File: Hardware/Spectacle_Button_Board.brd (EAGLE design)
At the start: 44.5 x 73.7 mm, 45 parts, among them J17 AUDIO-JACK3, J19 FTDI_DEVICE, U1 CY8C4146LQI-S422, U2 3.3V/150mA

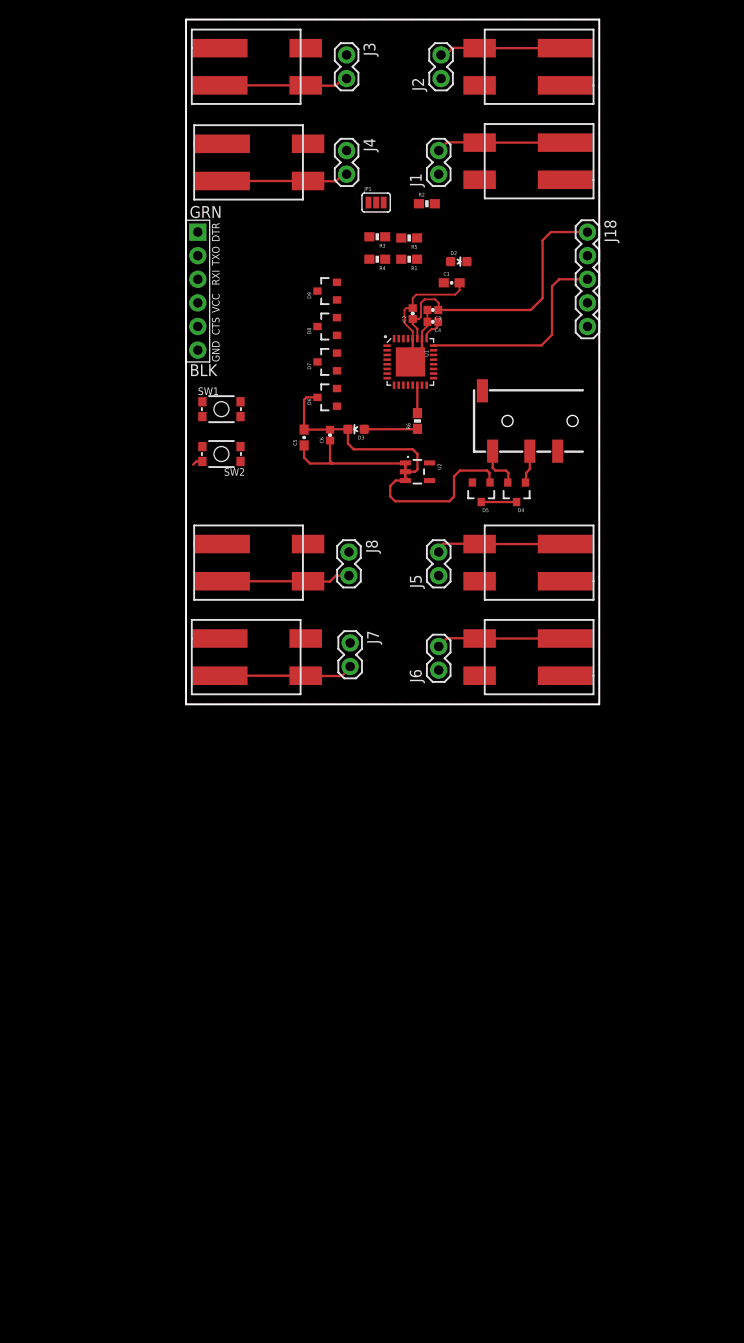
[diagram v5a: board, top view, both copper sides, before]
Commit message: Added second trrs connector
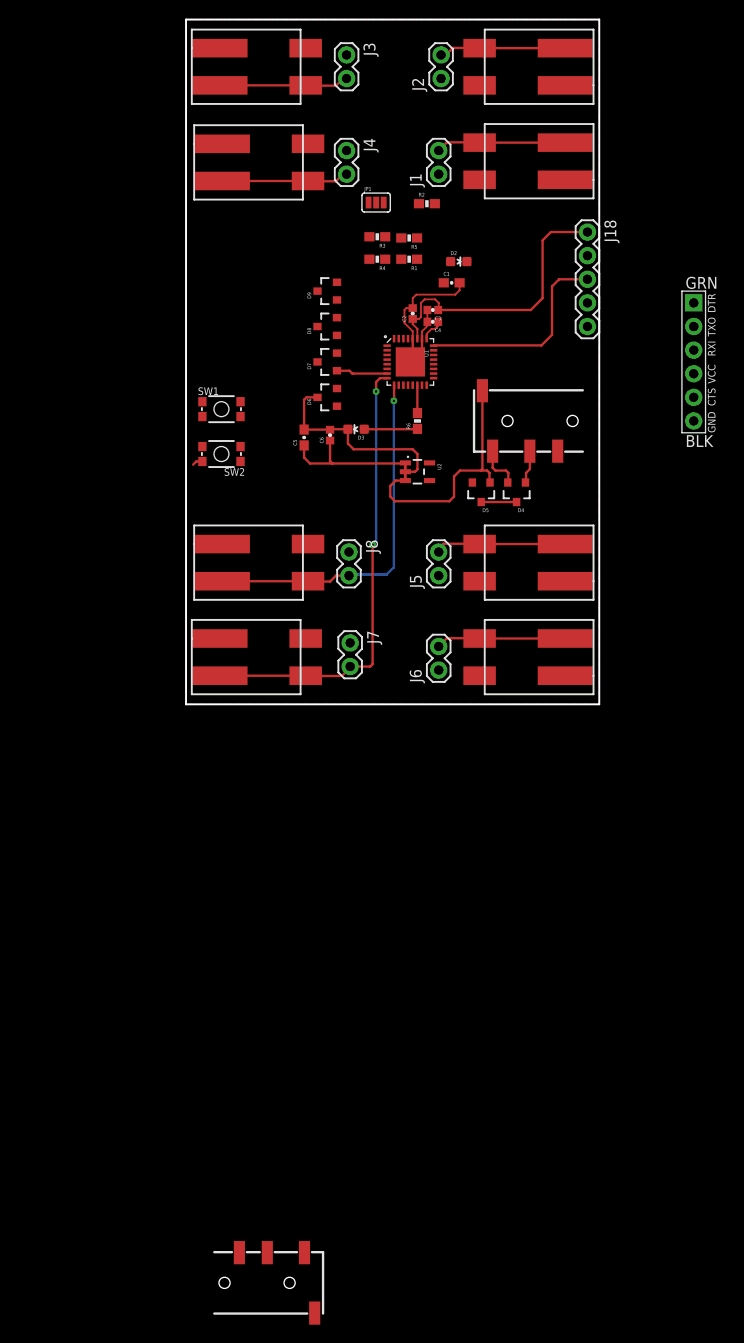
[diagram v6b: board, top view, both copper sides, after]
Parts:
- added J20: AUDIO-JACK3, SparkFun-Connectors:AUDIO-JACK-TRRS-SMD
- moved J19 53.9 mm to (22.9, 27.9)
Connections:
- net GND: now also J20.RING2
- net VIN: now also J20.EARTH
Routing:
- net IN_6: track 14.5 -> 48.9 mm, vias 0 -> 2
- net IN_7: track 13.9 -> 38.7 mm, vias 0 -> 1
- net VIN: track 34.6 -> 43.3 mm
- net IN_5: track 14.0 -> 19.6 mm
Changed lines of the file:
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@@
 <element name="JP1" library="SparkFun-Passives" package="PAD-JUMPER-3-NC_BY_PASTE_YES_SILK_FULL_BOX" value="JUMPER-PAD-3-NC_BY_PASTE" x="-11.303" y="45.085"/>
 <element name="J18" library="SparkFun-Connectors" package="1X05" value="" x="11.43" y="41.91" rot="R270"/>
-<element name="J19" library="SparkFun-Connectors" package="FTDI_DEVICE_SIDE" value="FTDI_DEVICE" x="-30.48" y="35.56" rot="R270"/>
+<element name="J19" library="SparkFun-Connectors" package="FTDI_DEVICE_SIDE" value="FTDI_DEVICE" x="22.86" y="27.94" rot="R270"/>
 <element name="D2" library="SparkFun-LED" package="LED-0603" value="RED" x="-2.413" y="38.735" rot="R270">
 <attribute name="PROD_ID" value="DIO-00819" x="-2.413" y="38.735" size="1.778" layer="27" font="vector" ratio="15" rot="R270" display="off"/>
@@
 <attribute name="PROD_ID" value="DIO-12501" x="-16.51" y="35.56" size="1.778" layer="27" font="vector" ratio="15" rot="R90" display="off"/>
 </element>
+<element name="J20" library="SparkFun-Connectors" package="AUDIO-JACK-TRRS-SMD" value="AUDIO-JACK3" x="-29.21" y="-71.12"/>
 </elements>
 <signals>
@@
 <vertex x="12.7" y="64.77"/>
 </polygon>
+<contactref element="J20" pad="RING2"/>
+<wire x1="-28.13" y1="-1.81" x2="-26.01" y2="-67.87" width="0" layer="19" extent="1-1"/>
+<wire x1="-18.88" y1="-1.81" x2="-28.13" y2="-1.81" width="0" layer="19" extent="1-1"/>
+<wire x1="-14.097" y1="-2.286" x2="-18.88" y2="-1.81" width="0" layer="19" extent="1-1"/>
+<wire x1="-14.224" y1="7.493" x2="-14.097" y2="-2.286" width="0" layer="19" extent="1-1"/>
+<wire x1="-18.626" y1="8.35" x2="-14.224" y2="7.493" width="0" layer="19" extent="1-1"/>
+<wire x1="-27.876" y1="8.35" x2="-18.626" y2="8.35" width="0" layer="19" extent="1-1"/>
+<wire x1="-30.988" y1="16.891" x2="-27.876" y2="8.35" width="0" layer="19" extent="1-1"/>
+<wire x1="-25.89" y1="23.66" x2="-29.99" y2="17.234" width="0" layer="19" extent="1-1"/>
+<wire x1="-19.05" y1="23.876" x2="-25.89" y2="23.66" width="0" layer="19" extent="1-1"/>
+<wire x1="-17.61" y1="27.94" x2="-17.61" y2="24.13" width="0" layer="19" extent="1-1"/>
+<wire x1="-17.61" y1="31.75" x2="-17.61" y2="27.94" width="0" layer="19" extent="1-1"/>
+<wire x1="-17.61" y1="35.56" x2="-17.61" y2="31.75" width="0" layer="19" extent="1-1"/>
+<wire x1="0" y1="12.87" x2="-6.858" y2="16.383" width="0" layer="19" extent="1-1"/>
+<wire x1="8.23" y1="18.34" x2="3.81" y2="12.87" width="0" layer="19" extent="1-1"/>
+<wire x1="-0.17" y1="4.35" x2="0" y2="12.87" width="0" layer="19" extent="1-1"/>
+<wire x1="-4.572" y1="4.953" x2="-0.17" y2="4.35" width="0" layer="19" extent="1-1"/>
+<wire x1="9.08" y1="4.35" x2="-0.17" y2="4.35" width="0" layer="19" extent="1-1"/>
+<wire x1="-8.255" y1="32.131" x2="-17.61" y2="31.75" width="0" layer="19" extent="1-1"/>
+<wire x1="-1.536" y1="38.735" x2="-2.325" y2="36.449" width="0" layer="19" extent="1-1"/>
+<wire x1="-0.17" y1="47.53" x2="-1.536" y2="38.735" width="0" layer="19" extent="1-1"/>
+<wire x1="-4.572" y1="48.133" x2="-0.17" y2="47.53" width="0" layer="19" extent="1-1"/>
+<wire x1="9.08" y1="47.53" x2="-0.17" y2="47.53" width="0" layer="19" extent="1-1"/>
+<wire x1="11.43" y1="39.37" x2="9.08" y2="47.53" width="0" layer="19" extent="1-1"/>
+<wire x1="-4.572" y1="-5.207" x2="-14.097" y2="-2.286" width="0" layer="19" extent="1-1"/>
+<wire x1="-0.17" y1="-5.81" x2="-4.572" y2="-5.207" width="0" layer="19" extent="1-1"/>
+<wire x1="9.08" y1="-5.81" x2="-0.17" y2="-5.81" width="0" layer="19" extent="1-1"/>
+<wire x1="9.08" y1="57.69" x2="9.08" y2="47.53" width="0" layer="19" extent="1-1"/>
+<wire x1="-0.17" y1="57.69" x2="9.08" y2="57.69" width="0" layer="19" extent="1-1"/>
+<wire x1="-4.318" y1="58.42" x2="-0.17" y2="57.69" width="0" layer="19" extent="1-1"/>
+<wire x1="-14.478" y1="50.673" x2="-4.572" y2="48.133" width="0" layer="19" extent="1-1"/>
+<wire x1="-18.626" y1="51.403" x2="-14.478" y2="50.673" width="0" layer="19" extent="1-1"/>
+<wire x1="-27.876" y1="51.403" x2="-18.626" y2="51.403" width="0" layer="19" extent="1-1"/>
+<wire x1="-14.478" y1="60.96" x2="-14.478" y2="50.673" width="0" layer="19" extent="1-1"/>
+<wire x1="-18.88" y1="61.69" x2="-14.478" y2="60.96" width="0" layer="19" extent="1-1"/>
+<wire x1="-28.13" y1="61.69" x2="-18.88" y2="61.69" width="0" layer="19" extent="1-1"/>
+<wire x1="22.86" y1="21.59" x2="8.23" y2="18.34" width="0" layer="19" extent="1-1"/>
+<wire x1="22.86" y1="24.13" x2="22.86" y2="21.59" width="0" layer="19" extent="1-1"/>
 </signal>
 <signal name="IN_0">
@@
 <wire x1="-16.256" y1="4.318" x2="-18.594" y2="4.318" width="0.254" layer="1"/>
 <wire x1="-18.594" y1="4.318" x2="-18.626" y2="4.35" width="0.254" layer="1"/>
-<wire x1="-15.51" y1="34.61" x2="-9.37" y2="25.44" width="0" layer="19" extent="1-1"/>
-<wire x1="-14.224" y1="4.953" x2="-9.37" y2="25.44" width="0" layer="19" extent="1-1"/>
+<wire x1="-9.37" y1="25.44" x2="-9.37" y2="23.777" width="0.254" layer="1"/>
+<wire x1="-9.37" y1="23.777" x2="-9.398" y2="23.749" width="0.254" layer="1"/>
+<via x="-9.398" y="23.749" extent="1-16" drill="0.254"/>
+<wire x1="-9.398" y1="23.749" x2="-9.398" y2="5.842" width="0.254" layer="16"/>
+<wire x1="-9.398" y1="5.842" x2="-10.16" y2="5.08" width="0.254" layer="16"/>
+<wire x1="-10.16" y1="5.08" x2="-14.097" y2="5.08" width="0.254" layer="16"/>
+<wire x1="-14.097" y1="5.08" x2="-14.224" y2="4.953" width="0.254" layer="16"/>
+<wire x1="-9.37" y1="25.44" x2="-15.51" y2="34.61" width="0" layer="19" extent="1-1"/>
 </signal>
 <signal name="IN_5">
@@
 <wire x1="-0.202" y1="-1.778" x2="-0.17" y2="-1.81" width="0.254" layer="1"/>
 <wire x1="-0.17" y1="-1.81" x2="9.08" y2="-1.81" width="0.254" layer="1"/>
-<wire x1="-15.51" y1="26.99" x2="-10.12" y2="26.69" width="0" layer="19" extent="1-1"/>
 <wire x1="-3.683" y1="-1.778" x2="-10.12" y2="26.69" width="0" layer="19" extent="1-1"/>
+<wire x1="-15.51" y1="26.99" x2="-14.163" y2="26.99" width="0.254" layer="1"/>
+<wire x1="-14.163" y1="26.99" x2="-13.843" y2="26.67" width="0.254" layer="1"/>
+<wire x1="-10.12" y1="26.69" x2="-13.823" y2="26.69" width="0.254" layer="1"/>
+<wire x1="-13.823" y1="26.69" x2="-13.843" y2="26.67" width="0.254" layer="1"/>
 </signal>
 <signal name="IN_4">
@@
 <wire x1="-28.13" y1="-5.81" x2="-18.88" y2="-5.81" width="0.254" layer="1"/>
 <wire x1="-10.12" y1="26.19" x2="-15.51" y2="36.51" width="0" layer="19" extent="1-1"/>
-<wire x1="-14.097" y1="-4.826" x2="-10.12" y2="26.19" width="0" layer="19" extent="1-1"/>
+<wire x1="-14.097" y1="-4.826" x2="-11.938" y2="-4.826" width="0.254" layer="1"/>
+<wire x1="-11.938" y1="-4.826" x2="-11.684" y2="-4.572" width="0.254" layer="1"/>
+<wire x1="-11.684" y1="-4.572" x2="-11.684" y2="8.255" width="0.254" layer="1"/>
+<via x="-11.684" y="8.255" extent="1-16" drill="0.254"/>
+<wire x1="-10.12" y1="26.19" x2="-10.894" y2="26.19" width="0.254" layer="1"/>
+<wire x1="-10.894" y1="26.19" x2="-11.303" y2="25.781" width="0.254" layer="1"/>
+<wire x1="-11.303" y1="25.781" x2="-11.303" y2="24.765" width="0.254" layer="1"/>
+<via x="-11.303" y="24.765" extent="1-16" drill="0.254"/>
+<wire x1="-11.303" y1="24.765" x2="-11.303" y2="8.636" width="0.254" layer="16"/>
+<wire x1="-11.303" y1="8.636" x2="-11.684" y2="8.255" width="0.254" layer="16"/>
 </signal>
 <signal name="VCC">
@@
 <wire x1="-2.921" y1="13.462" x2="-2.921" y2="15.621" width="0.254" layer="1"/>
 <wire x1="-2.921" y1="15.621" x2="-2.286" y2="16.256" width="0.254" layer="1"/>
-<wire x1="-2.286" y1="16.256" x2="0.635" y2="16.256" width="0.254" layer="1"/>
+<wire x1="-2.286" y1="16.256" x2="0" y2="16.256" width="0.254" layer="1"/>
+<wire x1="0" y1="16.256" x2="0.635" y2="16.256" width="0.254" layer="1"/>
 <wire x1="0.635" y1="16.256" x2="0.889" y2="16.002" width="0.254" layer="1"/>
 <wire x1="0.889" y1="16.002" x2="0.889" y2="15.031" width="0.254" layer="1"/>
 <wire x1="0.889" y1="15.031" x2="0.95" y2="14.97" width="0.254" layer="1"/>
-<wire x1="0.635" y1="16.256" x2="0.13" y2="24.84" width="0" layer="19" extent="1-1"/>
+<wire x1="0.13" y1="24.84" x2="0.13" y2="16.386" width="0.254" layer="1"/>
+<wire x1="0.13" y1="16.386" x2="0" y2="16.256" width="0.254" layer="1"/>
+<contactref element="J20" pad="EARTH"/>
+<wire x1="-9.271" y1="12.954" x2="-17.91" y2="-74.37" width="0" layer="19" extent="1-1"/>
 </signal>
 <signal name="N$2">
@@
 <contactref element="J19" pad="P$2"/>
 <contactref element="U1" pad="22"/>
-<wire x1="-30.48" y1="39.37" x2="-5.12" y2="28.69" width="0" layer="19" extent="1-1"/>
+<wire x1="22.86" y1="31.75" x2="-5.12" y2="28.69" width="0" layer="19" extent="1-1"/>
 </signal>
 <signal name="RXI">
 <contactref element="J19" pad="P$3"/>
 <contactref element="U1" pad="21"/>
-<wire x1="-30.48" y1="36.83" x2="-5.12" y2="28.19" width="0" layer="19" extent="1-1"/>
+<wire x1="22.86" y1="29.21" x2="-5.12" y2="28.19" width="0" layer="19" extent="1-1"/>
 </signal>
 <signal name="N$4">

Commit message: partially routed
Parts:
- moved J20 109.2 mm to (-31.8, 38.1)
- moved J17 43.6 mm to (-31.8, 27.9), turned to 0 degrees
- moved D5 33.6 mm to (-16.5, 43.2), turned to 90 degrees
- moved D4 32.5 mm to (-16.5, 39.4), turned to 90 degrees
- moved SW2 30.6 mm to (2.41, 22.2), turned to 90 degrees
- moved SW1 26.4 mm to (-1.52, 22.4), turned to 270 degrees
- moved J19 13.9 mm to (11.0, 20.6), turned to 90 degrees
- moved D6 11.4 mm to (-16.5, 35.6)
- moved D9 11.4 mm to (-16.5, 24.1)
- moved D2 2.84 mm to (-3.68, 41.3)
- moved R2 2.84 mm to (-3.30, 43.7)
- moved C1 2.59 mm to (-0.64, 35.9), turned to 180 degrees
- moved C4 0.40 mm to (-4.83, 32.4)
- moved C3 0.38 mm to (-4.83, 33.5)
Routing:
- net 3.3V: track 31.0 -> 79.1 mm, vias 0 -> 4
- net XRES: track 22.6 -> 40.5 mm, vias 0 -> 2
- net BTN: track 0.00 -> 15.0 mm, vias 0 -> 2
- net GND: track 48.8 -> 37.4 mm
- net N$3: track 0.00 -> 10.2 mm
- net IN_2: track 14.0 -> 23.4 mm
- net IN_3: track 13.7 -> 21.8 mm
- net IN_4: track 14.3 -> 20.9 mm
- net IN_7: track 38.7 -> 45.1 mm
- net VIN: track 43.3 -> 37.7 mm
- net SDA: track 4.77 -> 0.00 mm
- net IN_6: track 48.9 -> 53.3 mm
- net SCL: track 3.56 -> 0.00 mm
- net N$4: track 0.00 -> 2.34 mm
- net VCC: track 2.56 -> 3.29 mm

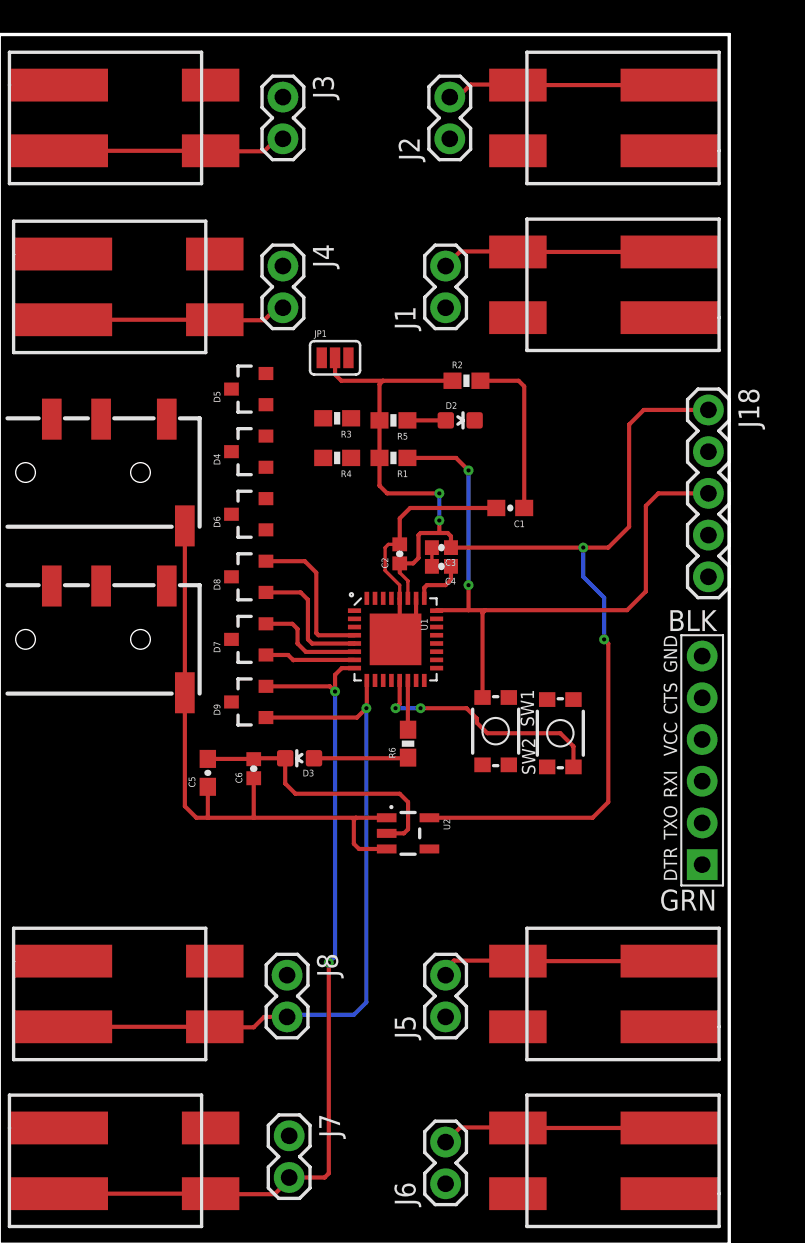
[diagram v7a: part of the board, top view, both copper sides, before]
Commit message: routed second half
pushing a lot of small changes because Eagle has been crashing and I
don't want to lose progress
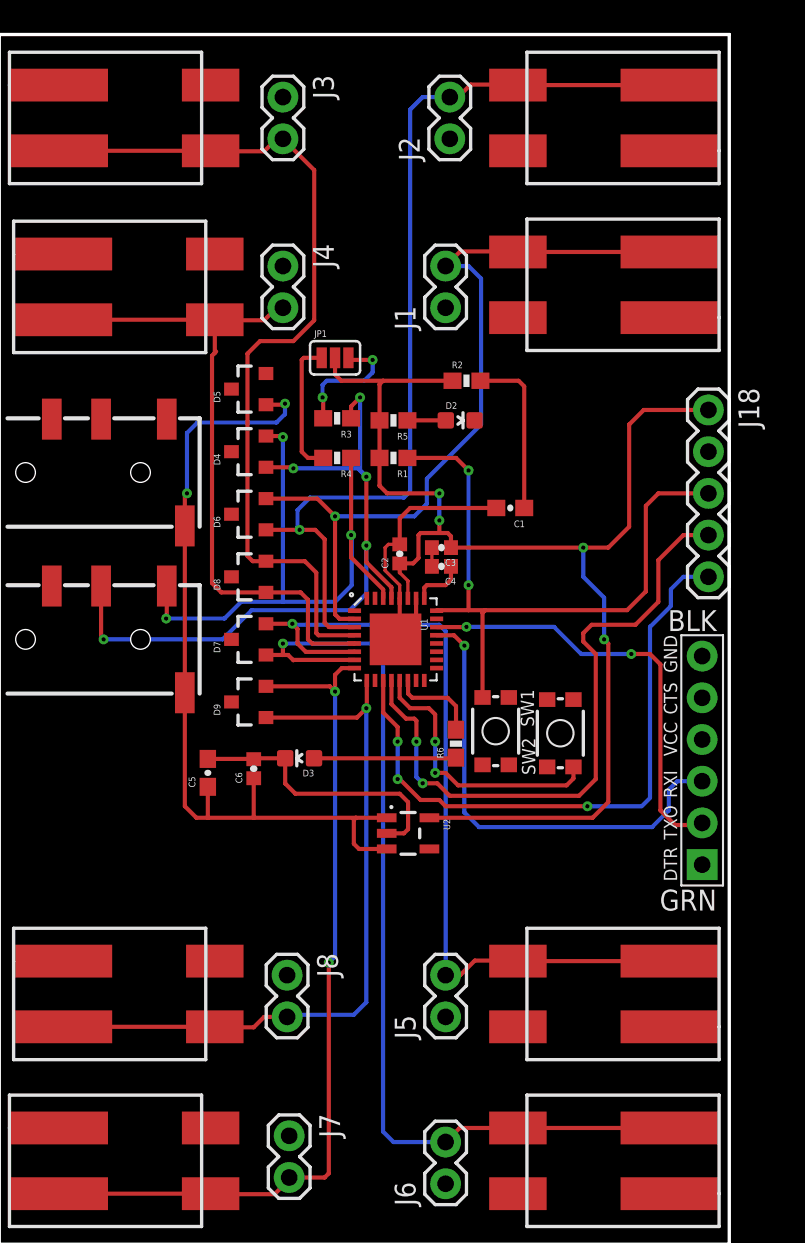
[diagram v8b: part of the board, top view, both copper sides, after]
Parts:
- moved R6 2.92 mm to (-3.94, 21.6)
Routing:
- net IN_1: track 13.7 -> 59.1 mm, vias 0 -> 1
- net SCL: track 0.00 -> 44.3 mm, vias 0 -> 5
- net IN_5: track 19.6 -> 59.8 mm, vias 0 -> 1
- net SWD_CLK: track 0.00 -> 39.4 mm, vias 0 -> 2
- net SWD_DATA: track 0.00 -> 38.5 mm, vias 0 -> 3
- net SDA: track 0.00 -> 37.7 mm, vias 0 -> 3
- net IN_0: track 14.0 -> 49.4 mm, vias 0 -> 1
- net IN_2: track 23.4 -> 53.7 mm
- net IN_4: track 20.9 -> 51.1 mm, vias 0 -> 1
- net RXI: track 0.00 -> 28.9 mm, vias 0 -> 1
- net TXO: track 0.00 -> 26.4 mm, vias 0 -> 2
- net IN_3: track 21.8 -> 41.6 mm
- net VIN: track 37.7 -> 51.7 mm, vias 0 -> 2
- net N$6: track 0.00 -> 8.33 mm
- net N$2: track 0.00 -> 7.70 mm, vias 0 -> 2
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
